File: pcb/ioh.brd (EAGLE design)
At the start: 100 x 80 mm, 27 parts, among them Q1 MOSFET-NCHANNEL2N7000, Q2 MOSFET-NCHANNEL2N7000, Q3 MOSFET-NCHANNEL2N7000, Q4 MOSFET-NCHANNEL2N7000

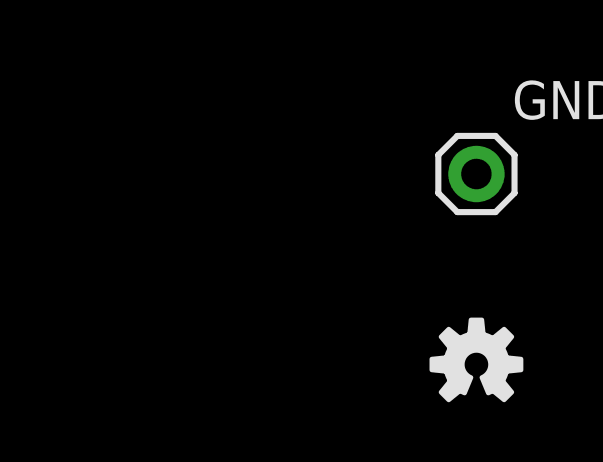
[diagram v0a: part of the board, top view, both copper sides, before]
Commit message: solder jumpers
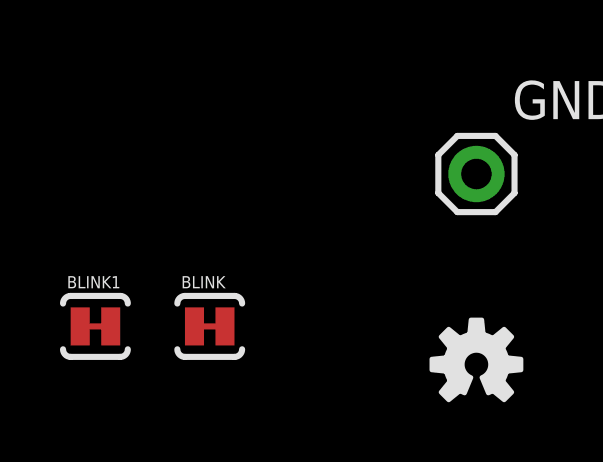
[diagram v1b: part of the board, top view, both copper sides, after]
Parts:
- added BLINK, BLINK1: JUMPER-PAD-2-NC_BY_TRACE, SparkFun-Passives:PAD-JUMPER-2-NC_BY_TRACE_YES_SILK
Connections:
- new net N$6: BLINK.2, Q1.2
- net BLINK: now also BLINK.1; no longer Q1.2
- net RXBACK: now also BLINK1.1, BLINK1.2
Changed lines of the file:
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@@
 <element name="GND" library="SparkFun-Connectors" package="1X01" value="M01PTH" x="-72.39" y="-83.82"/>
 <element name="LOGO1" library="SparkFun-Aesthetics" package="OSHW-LOGO-S" value="OSHW-LOGOS" x="-72.39" y="-90.17"/>
+<element name="BLINK" library="SparkFun-Passives" package="PAD-JUMPER-2-NC_BY_TRACE_YES_SILK" value="JUMPER-PAD-2-NC_BY_TRACE" x="-81.28" y="-88.9"/>
+<element name="BLINK1" library="SparkFun-Passives" package="PAD-JUMPER-2-NC_BY_TRACE_YES_SILK" value="JUMPER-PAD-2-NC_BY_TRACE" x="-85.09" y="-88.9"/>
 </elements>
 <signals>
@@
 <contactref element="JP1" pad="8"/>
 <contactref element="U$1" pad="8"/>
-<contactref element="Q1" pad="2"/>
-<wire x1="-52.07" y1="73.025" x2="-38.1" y2="62.23" width="0" layer="19" extent="1-1"/>
-<wire x1="-36.4" y1="13.62" x2="-38.1" y2="62.23" width="0" layer="19" extent="1-1"/>
+<contactref element="BLINK" pad="1"/>
+<wire x1="-36.4" y1="13.62" x2="-81.788" y2="-88.9" width="0" layer="19" extent="1-1"/>
+<wire x1="-38.1" y1="62.23" x2="-36.4" y2="13.62" width="0" layer="19" extent="1-1"/>
 </signal>
 <signal name="BLINK5">
-<contactref element="LED2" pad="DI"/>
 <contactref element="R1" pad="P$1"/>
 <contactref element="Q1" pad="3"/>
+<contactref element="LED2" pad="DI"/>
 <wire x1="-67.31" y1="69.85" x2="-50.8" y2="71.12" width="0" layer="19" extent="1-1"/>
 <wire x1="-47.53" y1="40.64" x2="-50.8" y2="71.12" width="0" layer="19" extent="1-1"/>
@@
 <contactref element="U$1" pad="14"/>
 <contactref element="JP2" pad="4"/>
+<contactref element="BLINK1" pad="1"/>
+<contactref element="BLINK1" pad="2"/>
+<wire x1="-84.582" y1="-88.9" x2="-85.598" y2="-88.9" width="0" layer="19" extent="1-1"/>
+<wire x1="-66.04" y1="-33.02" x2="-84.582" y2="-88.9" width="0" layer="19" extent="1-1"/>
 <wire x1="-14.4" y1="15.62" x2="-66.04" y2="-33.02" width="0" layer="19" extent="1-1"/>
 <wire x1="-30.48" y1="72.39" x2="-14.4" y2="15.62" width="0" layer="19" extent="1-1"/>
@@
 <wire x1="-59.7916" y1="-55.9308" x2="-72.2884" y2="-55.9308" width="0" layer="19" extent="1-1"/>
 </signal>
+<signal name="N$6">
+<contactref element="Q1" pad="2"/>
+<contactref element="BLINK" pad="2"/>
+<wire x1="-52.07" y1="73.025" x2="-80.772" y2="-88.9" width="0" layer="19" extent="1-1"/>
+</signal>
 </signals>
